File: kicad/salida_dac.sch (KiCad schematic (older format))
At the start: 39 parts, among them U5 4016, U6 4016, U7 4016, U7 TL064, U8 4016

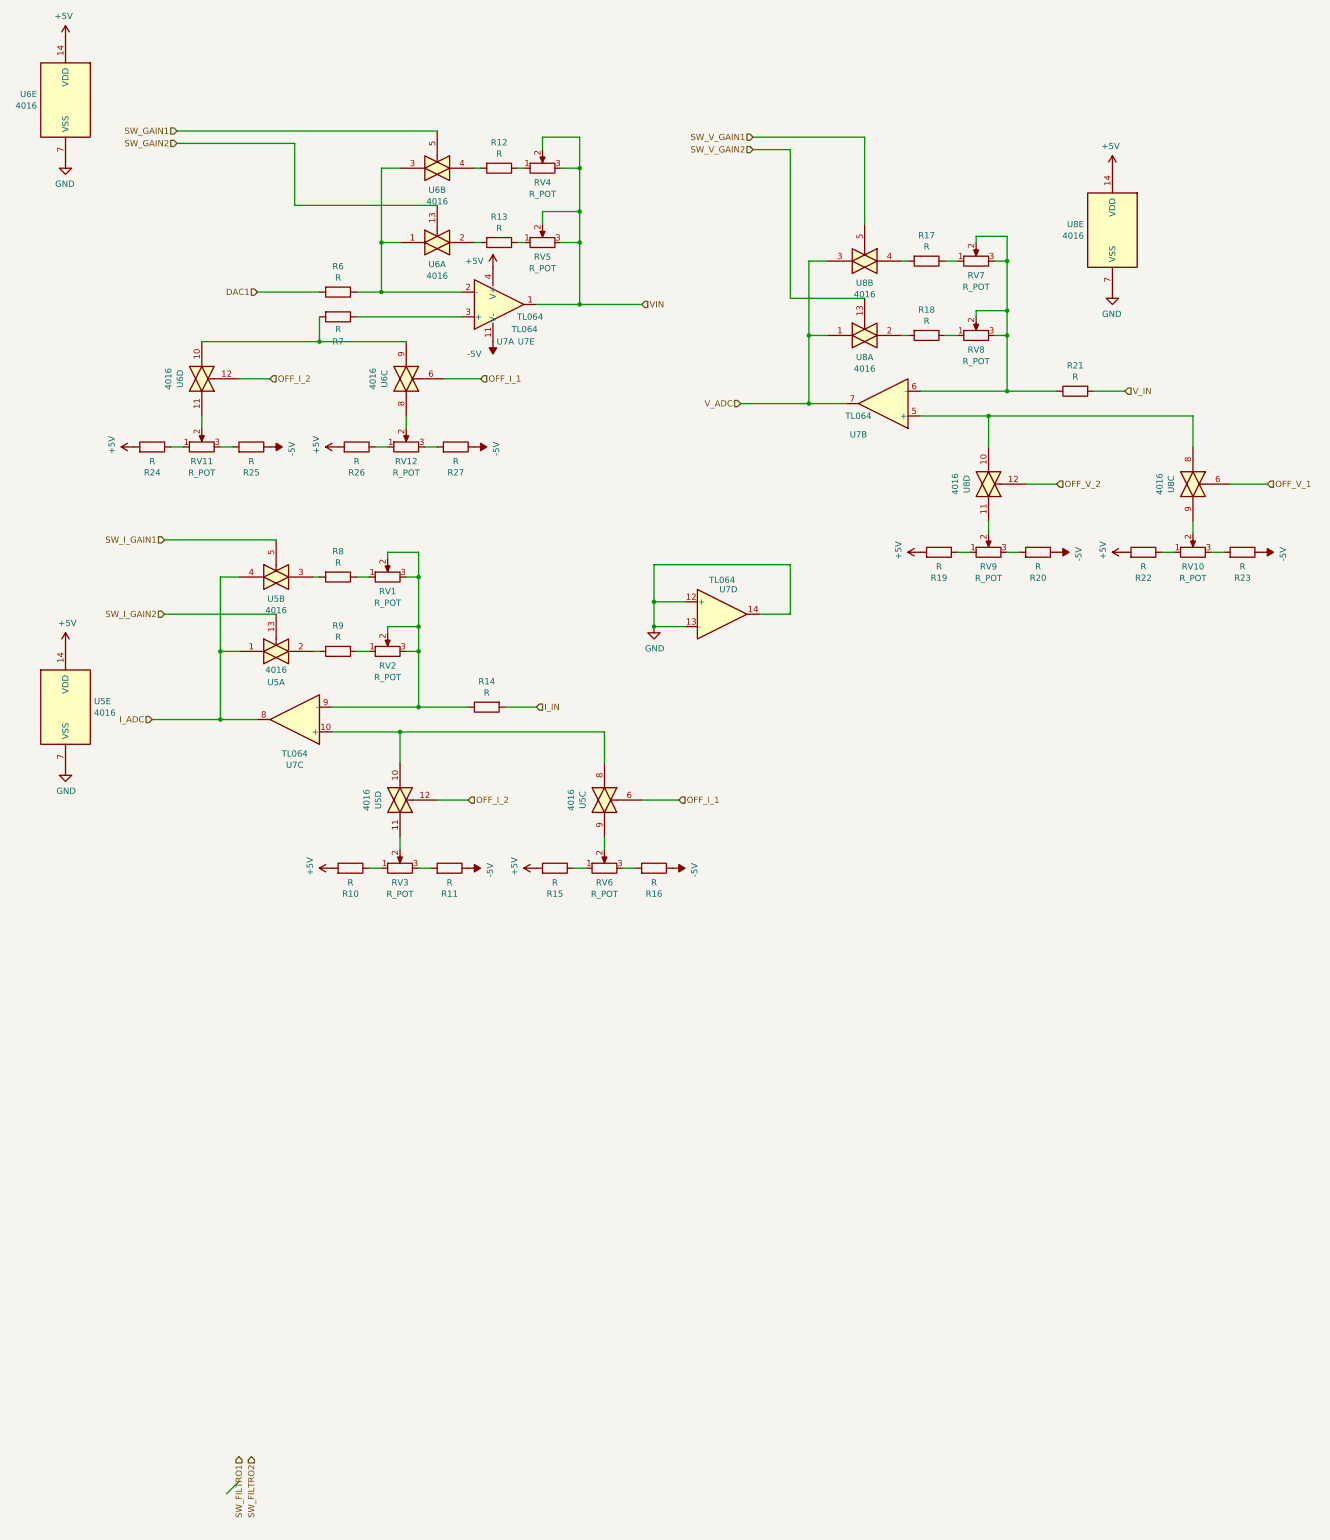
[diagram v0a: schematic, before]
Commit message: agregar identificador y comentarios a amplificadores
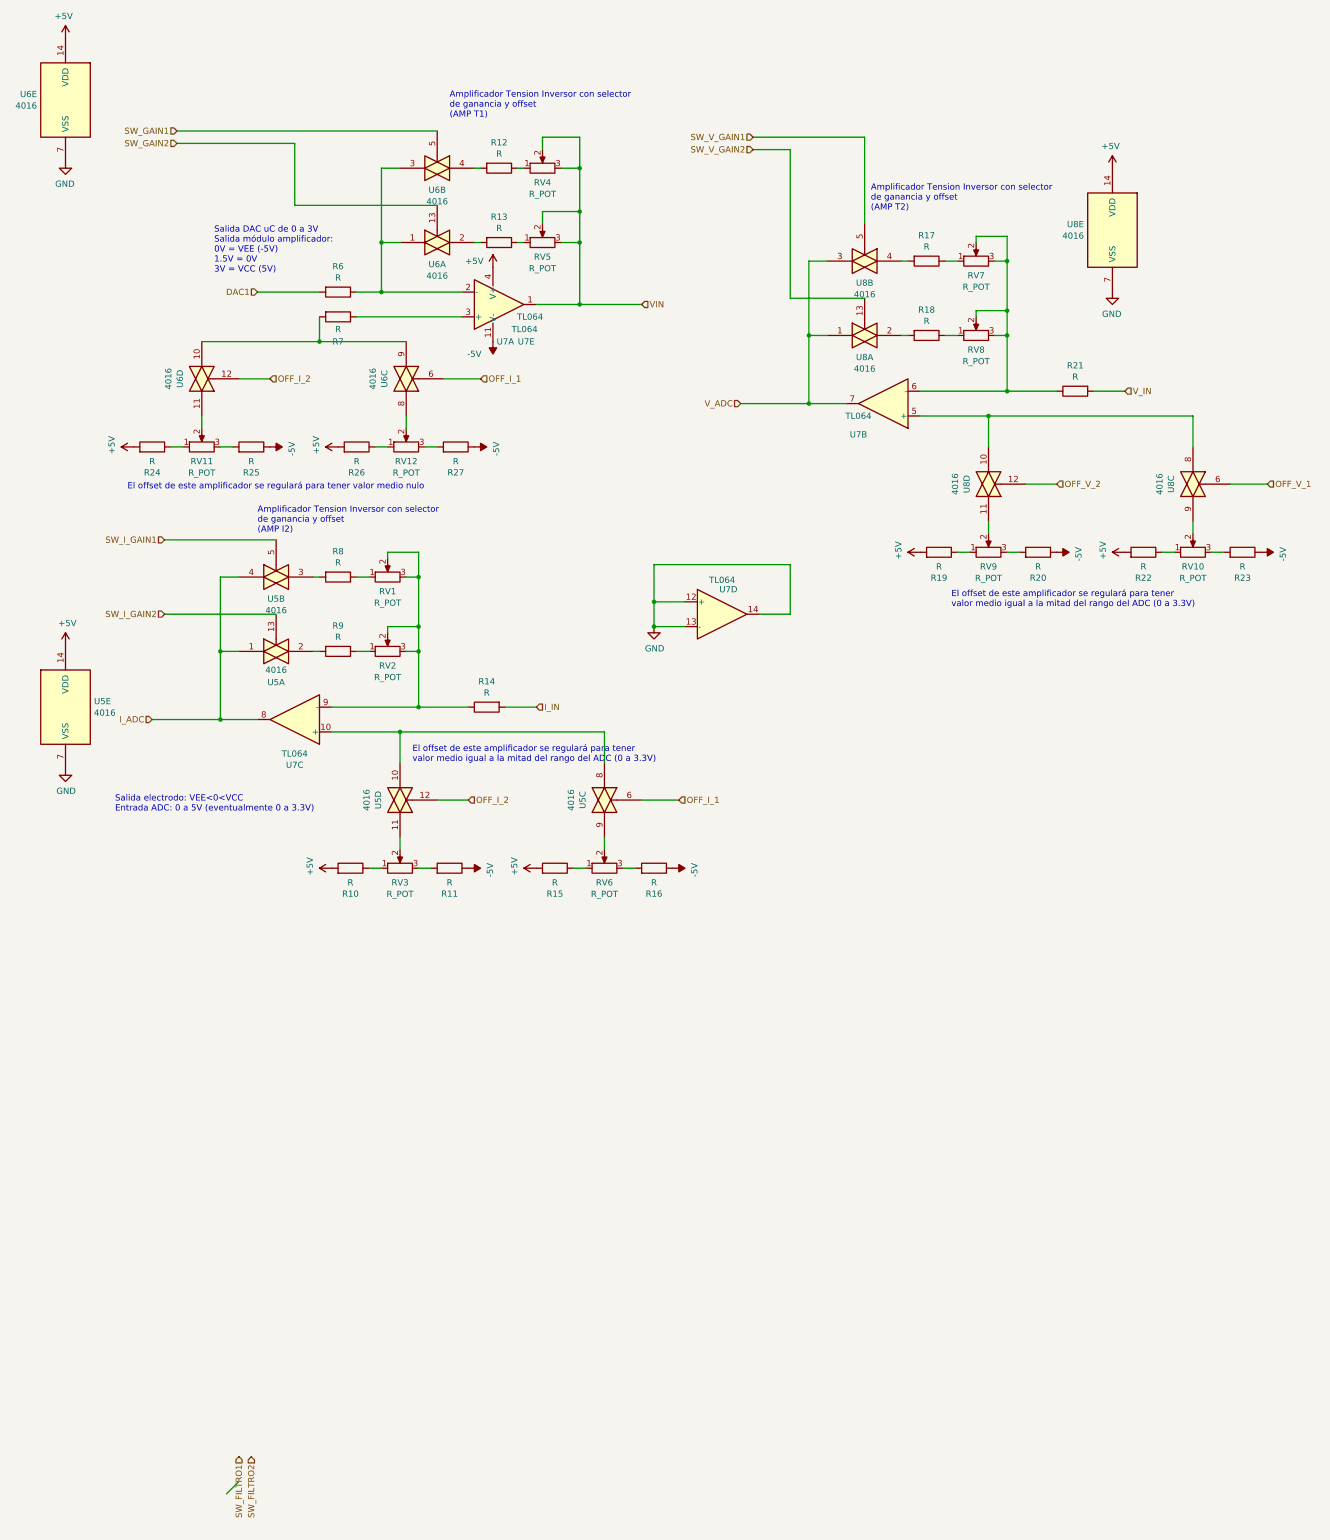
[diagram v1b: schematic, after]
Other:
- note added: "Amplificador Tension Inversor con selector\nde ganancia y offset\n(AMP I2)"
- note added: "Amplificador Tension Inversor con selector\nde ganancia y offset\n(AMP T1)"
- note added: "Amplificador Tension Inversor con selector\nde ganancia y offset\n(AMP T2)"
- note added: "El offset de este amplificador se regulará para tener valor medio nulo"
- note added: "El offset de este amplificador se regulará para tener\nvalor medio igual a la mitad del rango del ADC (0 a 3.3V)"
- note added: "Salida DAC uC de 0 a 3V\nSalida módulo amplificador:\n0V = VEE (-5V)\n1.5V = 0V\n3V = VCC (5V)"
- note added: "Salida electrodo: VEE<0<VCC\nEntrada ADC: 0 a 5V (eventualmente 0 a 3.3V)"
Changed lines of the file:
@@
 EESchema Schematic File Version 4
 LIBS:potenciostato-cache
-EELAYER 26 0
+EELAYER 29 0
 EELAYER END
 $Descr A4 11693 8268
@@
 Wire Wire Line
 	5750 5050 5750 5350
+Text Notes 2200 2700 0    50   ~ 0
+Salida DAC uC de 0 a 3V\nSalida módulo amplificador:\n0V = VEE (-5V)\n1.5V = 0V\n3V = VCC (5V)
+Text Notes 1400 7050 0    50   ~ 0
+Salida electrodo: VEE<0<VCC\nEntrada ADC: 0 a 5V (eventualmente 0 a 3.3V)
+Text Notes 2550 4800 0    50   ~ 0
+Amplificador Tension Inversor con selector\nde ganancia y offset\n(AMP I2)
+Text Notes 4100 1450 0    50   ~ 0
+Amplificador Tension Inversor con selector\nde ganancia y offset\n(AMP T1)
+Text Notes 7500 2200 0    50   ~ 0
+Amplificador Tension Inversor con selector\nde ganancia y offset\n(AMP T2)
+Text Notes 1500 4450 0    50   ~ 0
+El offset de este amplificador se regulará para tener valor medio nulo
+Text Notes 8150 5400 0    50   ~ 0
+El offset de este amplificador se regulará para tener\nvalor medio igual a la mitad del rango del ADC (0 a 3.3V)
+Text Notes 3800 6650 0    50   ~ 0
+El offset de este amplificador se regulará para tener\nvalor medio igual a la mitad del rango del ADC (0 a 3.3V)
 $EndSCHEMATC

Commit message: Modificaciones en schematic
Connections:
- net OFF_I_1: no longer U6.6
- net OFF_I_2: no longer U6.12
- new net OFF_DAC_1: U6.6
- new net OFF_DAC_2: U6.12
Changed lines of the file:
@@
 EESchema Schematic File Version 4
-LIBS:potenciostato-cache
-EELAYER 26 0
+EELAYER 30 0
 EELAYER END
 $Descr A4 11693 8268
@@
 $EndComp
 Text HLabel 2650 3550 2    50   Input ~ 0
-OFF_I_2
+OFF_DAC_2
 Wire Wire Line
 	2650 3550 2400 3550
 Text HLabel 4350 3550 2    50   Input ~ 0
-OFF_I_1
+OFF_DAC_1
 Wire Wire Line
 	4350 3550 4050 3550
@@
 Text Notes 1400 7050 0    50   ~ 0
 Salida electrodo: VEE<0<VCC\nEntrada ADC: 0 a 5V (eventualmente 0 a 3.3V)
-Text Notes 2550 4800 0    50   ~ 0
-Amplificador Tension Inversor con selector\nde ganancia y offset\n(AMP I2)
 Text Notes 4100 1450 0    50   ~ 0
 Amplificador Tension Inversor con selector\nde ganancia y offset\n(AMP T1)
@@
 Text Notes 3800 6650 0    50   ~ 0
 El offset de este amplificador se regulará para tener\nvalor medio igual a la mitad del rango del ADC (0 a 3.3V)
+Text Notes 2550 4800 0    50   ~ 0
+Amplificador Tension Inversor con selector\nde ganancia y offset\n(AMP I2)
 $EndSCHEMATC

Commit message: prueba
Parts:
- R1, R11, R15, R16, R2, R25, R27, R5, R6, R9: value R -> 1K; symbol Device:R -> salida_dac-rescue:R-Device
- R10, R14, R17, R18, R24, R26: value R -> 10K; symbol Device:R -> salida_dac-rescue:R-Device
- R12, R3, R7: value R -> 3K3; symbol Device:R -> salida_dac-rescue:R-Device
- R13, R4, R8: value R -> 4K7; symbol Device:R -> salida_dac-rescue:R-Device
- RV1, RV2, RV4, RV5: symbol Device:R_POT -> salida_dac-rescue:R_POT-Device
- RV10, RV11, RV12, RV3, RV6, RV7, RV8, RV9: value R_POT -> 1K; symbol Device:R_POT -> salida_dac-rescue:R_POT-Device
- U5, U6, U7, U8: symbol 4xxx:4016 -> salida_dac-rescue:4016-4xxx
- U7: symbol Amplifier_Operational:TL064 -> salida_dac-rescue:TL064-Amplifier_Operational

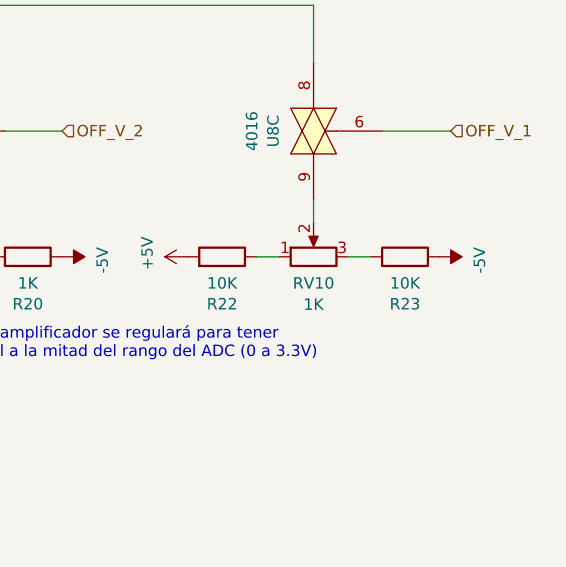
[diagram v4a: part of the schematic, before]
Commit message: modificamos R22 que estaba mal anotada
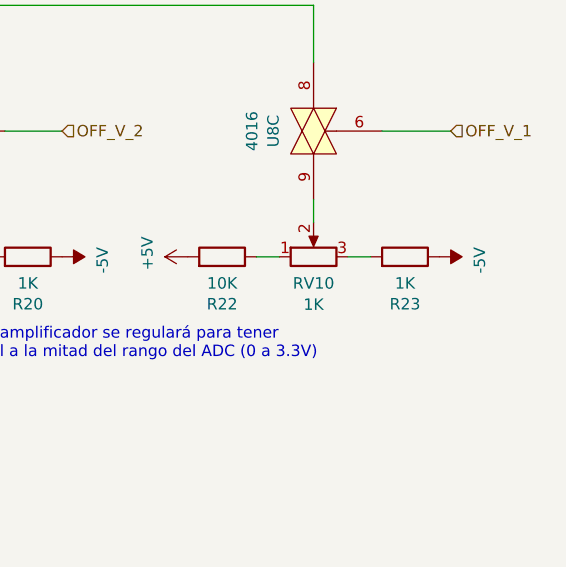
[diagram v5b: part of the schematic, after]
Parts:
- R18: value 10K -> 1K
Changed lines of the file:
@@
 $Descr A4 11693 8268
 encoding utf-8
-Sheet 1 1
+Sheet 2 3
 Title ""
 Date ""
@@
 AR Path="/6013BA2D/5F9D897F" Ref="R23"  Part="1"
 F 0 "R23" V 10293 4950 50  0000 C CNN
-F 1 "10K" V 10384 4950 50  0000 C CNN
+F 1 "1K" V 10384 4950 50  0000 C CNN
 F 2 "Resistor_THT:R_Axial_DIN0207_L6.3mm_D2.5mm_P7.62mm_Horizontal" V 10430 4950 50  0001 C CNN
 F 3 "~" H 10500 4950 50  0001 C CNN

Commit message: modificaciones finales al kickad
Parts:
- R18, R25: value 1K -> 15K
- R5: value 1K -> 10K
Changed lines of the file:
@@
 AR Path="/6013BA2D/5F98484D" Ref="R10"  Part="1"
 F 0 "R10" V 3093 7500 50  0000 C CNN
-F 1 "1K" V 3184 7500 50  0000 C CNN
+F 1 "10K" V 3184 7500 50  0000 C CNN
 F 2 "Resistor_THT:R_Axial_DIN0207_L6.3mm_D2.5mm_P7.62mm_Horizontal" V 3230 7500 50  0001 C CNN
 F 3 "~" H 3300 7500 50  0001 C CNN
@@
 AR Path="/6013BA2D/5F9D897F" Ref="R23"  Part="1"
 F 0 "R23" V 10293 4950 50  0000 C CNN
-F 1 "1K" V 10384 4950 50  0000 C CNN
+F 1 "15K" V 10384 4950 50  0000 C CNN
 F 2 "Resistor_THT:R_Axial_DIN0207_L6.3mm_D2.5mm_P7.62mm_Horizontal" V 10430 4950 50  0001 C CNN
 F 3 "~" H 10500 4950 50  0001 C CNN
@@
 AR Path="/6013BA2D/605448F1" Ref="R25"  Part="1"
 F 0 "R25" V 2293 4100 50  0000 C CNN
-F 1 "1K" V 2384 4100 50  0000 C CNN
+F 1 "15K" V 2384 4100 50  0000 C CNN
 F 2 "Resistor_THT:R_Axial_DIN0207_L6.3mm_D2.5mm_P7.62mm_Horizontal" V 2430 4100 50  0001 C CNN
 F 3 "~" H 2500 4100 50  0001 C CNN
